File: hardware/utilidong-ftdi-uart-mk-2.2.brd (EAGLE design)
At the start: 20.3 x 17.8 mm, 14 parts, among them U1 FTS31XS

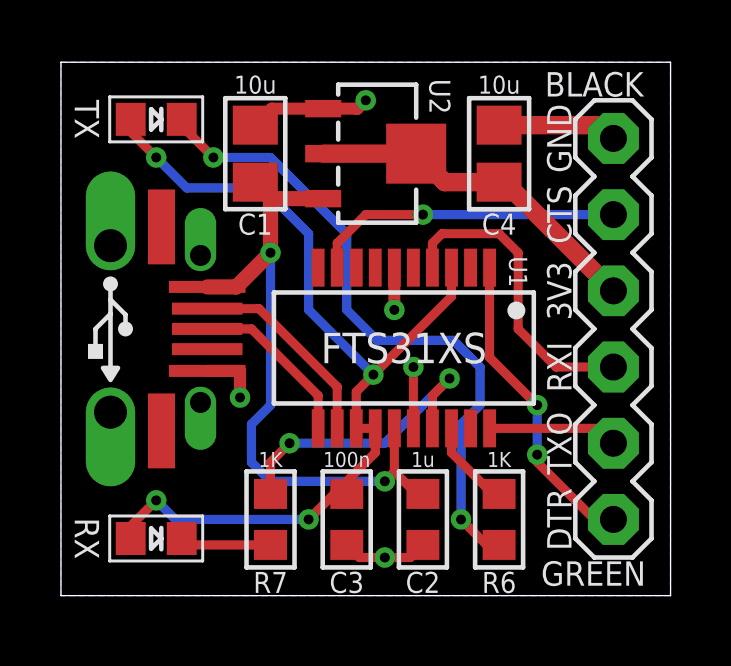
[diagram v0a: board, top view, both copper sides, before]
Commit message: almost finished way smaller form factor, now flipped to the correct orientation
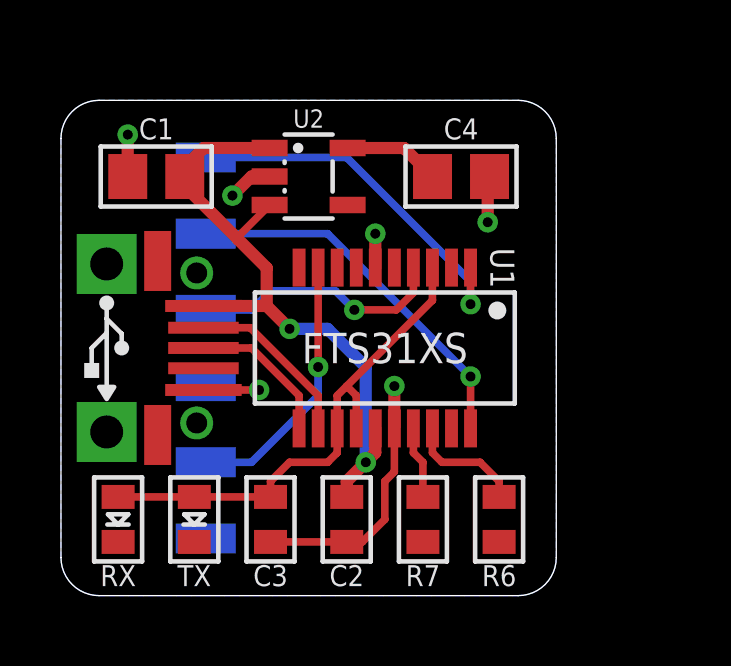
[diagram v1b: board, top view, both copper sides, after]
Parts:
- removed U$3: (no value), A_butts:COW_SMALL
- C2, C3: device a_parts:C0603 -> a_parts:C0603-TIGHTER
- R6, R7: device a_parts:R0603 -> a_parts:R0603-TIGHTER
- RX, TX: value LED0603 -> LED0603-TIGHT; device a_parts:LED-0603 -> a_parts:LED-0603-TIGHT
- U2: value (none) -> V_REG_SOT-23-5SPX3819; device a_parts:SOT89 -> a_parts:SOT23-5
- UART: value FTDI_3V3 -> FTDI_CONNSMT_FEMALE_RA_3V3_FLIPPED; device a_parts:FTDI_3V3 -> a_parts:FTDI_CONN_SMT_FEMALE_RA_3V3_FLIPPED
- USB: value (none) -> USB-AB-SHIELDFCI-10103594-USB-MICRO-B-EVENLESS; device a_parts:FCI-10103594-USB-MICRO-B-LESS -> a_parts:FCI-101035840-USB-MICRO-B-EVENLESS
- moved UART 13.6 mm to (4.83, 8.26), flipped to the bottom, turned to 180 degrees
- moved TX 13.4 mm to (4.45, 2.54), turned to 90 degrees
- moved R7 5.08 mm to (12.1, 2.54)
- moved C1 3.39 mm to (3.17, 14.0), turned to 180 degrees
- moved C3 2.54 mm to (6.99, 2.54)
- moved C2 2.54 mm to (9.53, 2.54)
- moved U2 2.41 mm to (8.26, 14.0)
- moved C4 1.48 mm to (13.3, 14.0), turned to 0 degrees
- moved RX 1.42 mm to (1.91, 2.54), turned to 90 degrees
- moved USB 0.65 mm to (1.52, 8.26)
- moved U1 0.63 mm to (10.8, 8.26)
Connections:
- net !CTS: now also UART.5; no longer UART.P$5
- net !DTR: now also UART.1; no longer UART.P$1
- net 3.3V: now also U2.5, UART.4; no longer U2.2, U2.4, UART.P$4
- net 5V: now also U2.1
- net GND: now also U2.2, UART.6; no longer U2.1, UART.P$6
- net RXI: now also UART.3; no longer UART.P$3
- net TXO: now also UART.2; no longer UART.P$2
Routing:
- net N$9: track 21.9 -> 0.00 mm, vias 2 -> 0
- net 3V3_INT: track 31.8 -> 17.2 mm, vias 4 -> 0
- net 3.3V: track 11.6 -> 3.22 mm
- net TXO: track 4.33 -> 12.5 mm, vias 0 -> 1
- net N$12: track 10.1 -> 2.42 mm, vias 2 -> 0
- net N$10: track 3.05 -> 0.00 mm
- net !DTR: track 10.5 -> 12.5 mm, vias 2 -> 1
- net RXI: track 10.3 -> 8.52 mm, vias 0 -> 1
- net !CTS: track 10.4 -> 8.93 mm
- net N$7: track 2.97 -> 3.95 mm
- net D-: track 6.80 -> 5.85 mm
- net D+: track 5.71 -> 4.94 mm
- net 5V: track 22.0 -> 22.5 mm
- net GND: track 16.3 -> 16.2 mm, vias 5 -> 6
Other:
- board size 20.3 x 17.8 mm -> 16.5 x 16.5 mm
- board text removed: "by schizobovine <sean@yak.net>"
